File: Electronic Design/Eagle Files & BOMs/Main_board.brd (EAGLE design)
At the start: 99.9 x 69 mm, 35 parts, among them IC2 ATMEGA328-PU, IC3 LM2596S, Q1 IRF9540, Q2 IRF9540, X1 16MHz

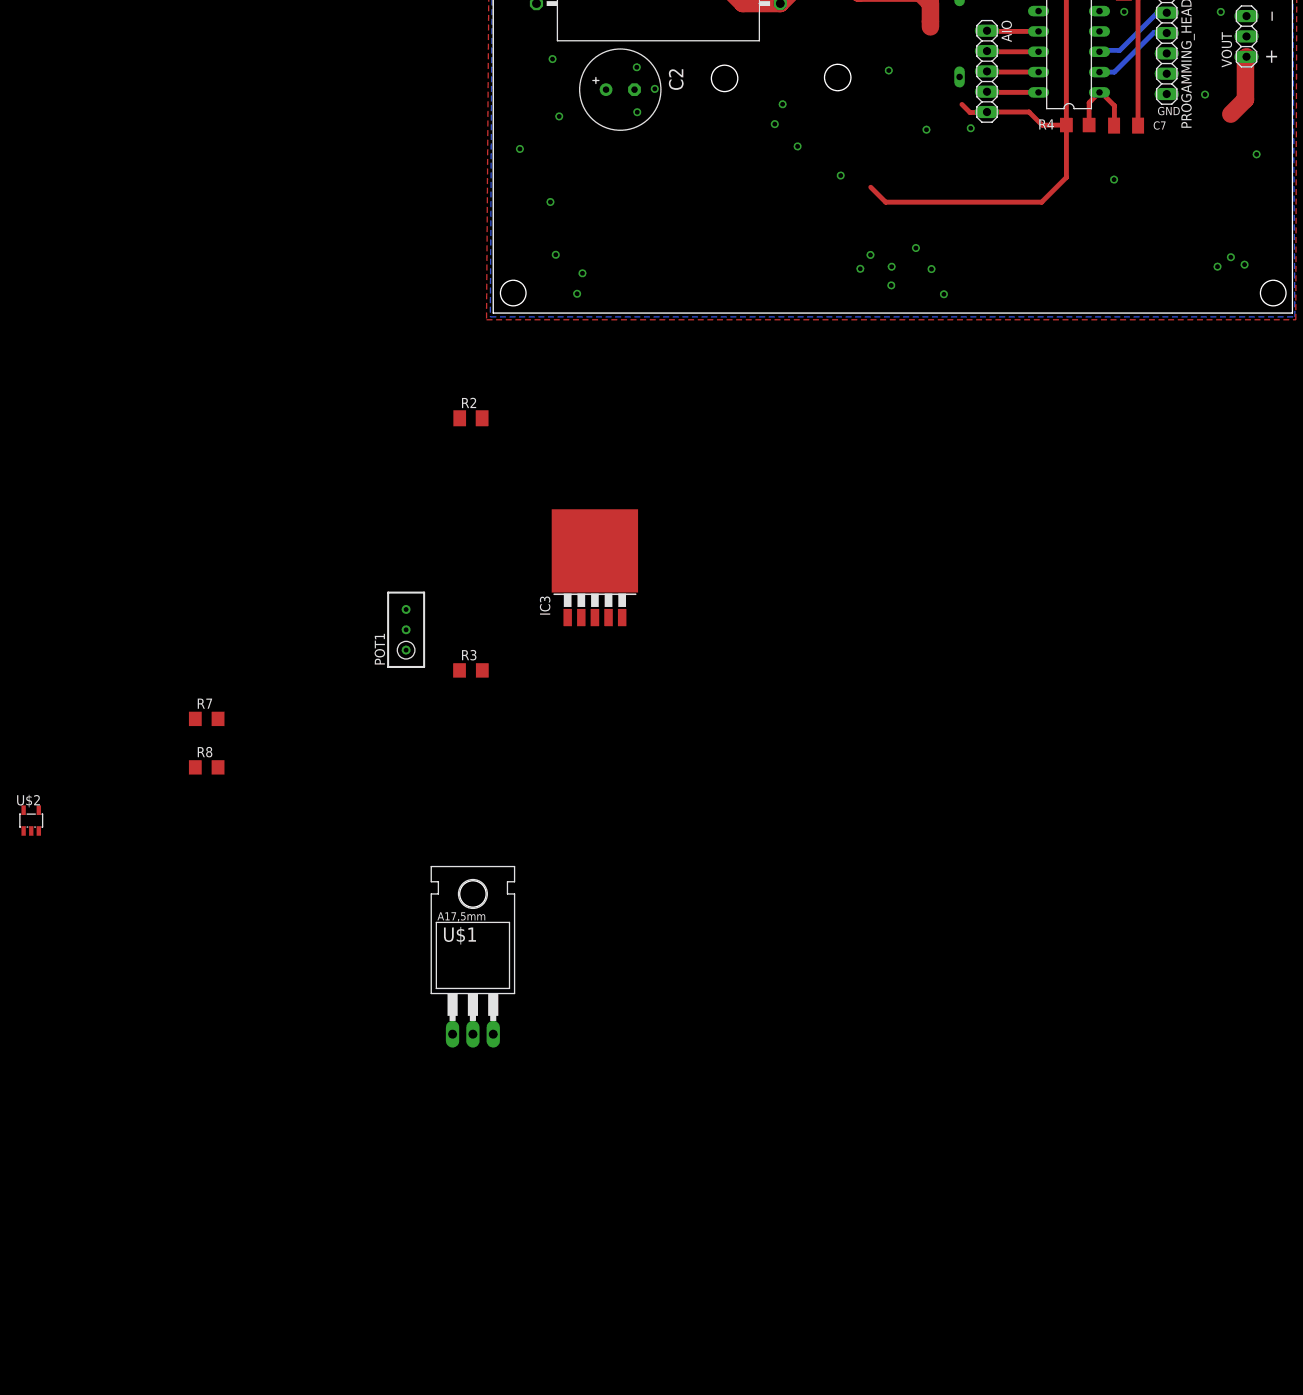
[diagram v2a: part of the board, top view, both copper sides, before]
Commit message: Adding in inductor and feedback to LM2576
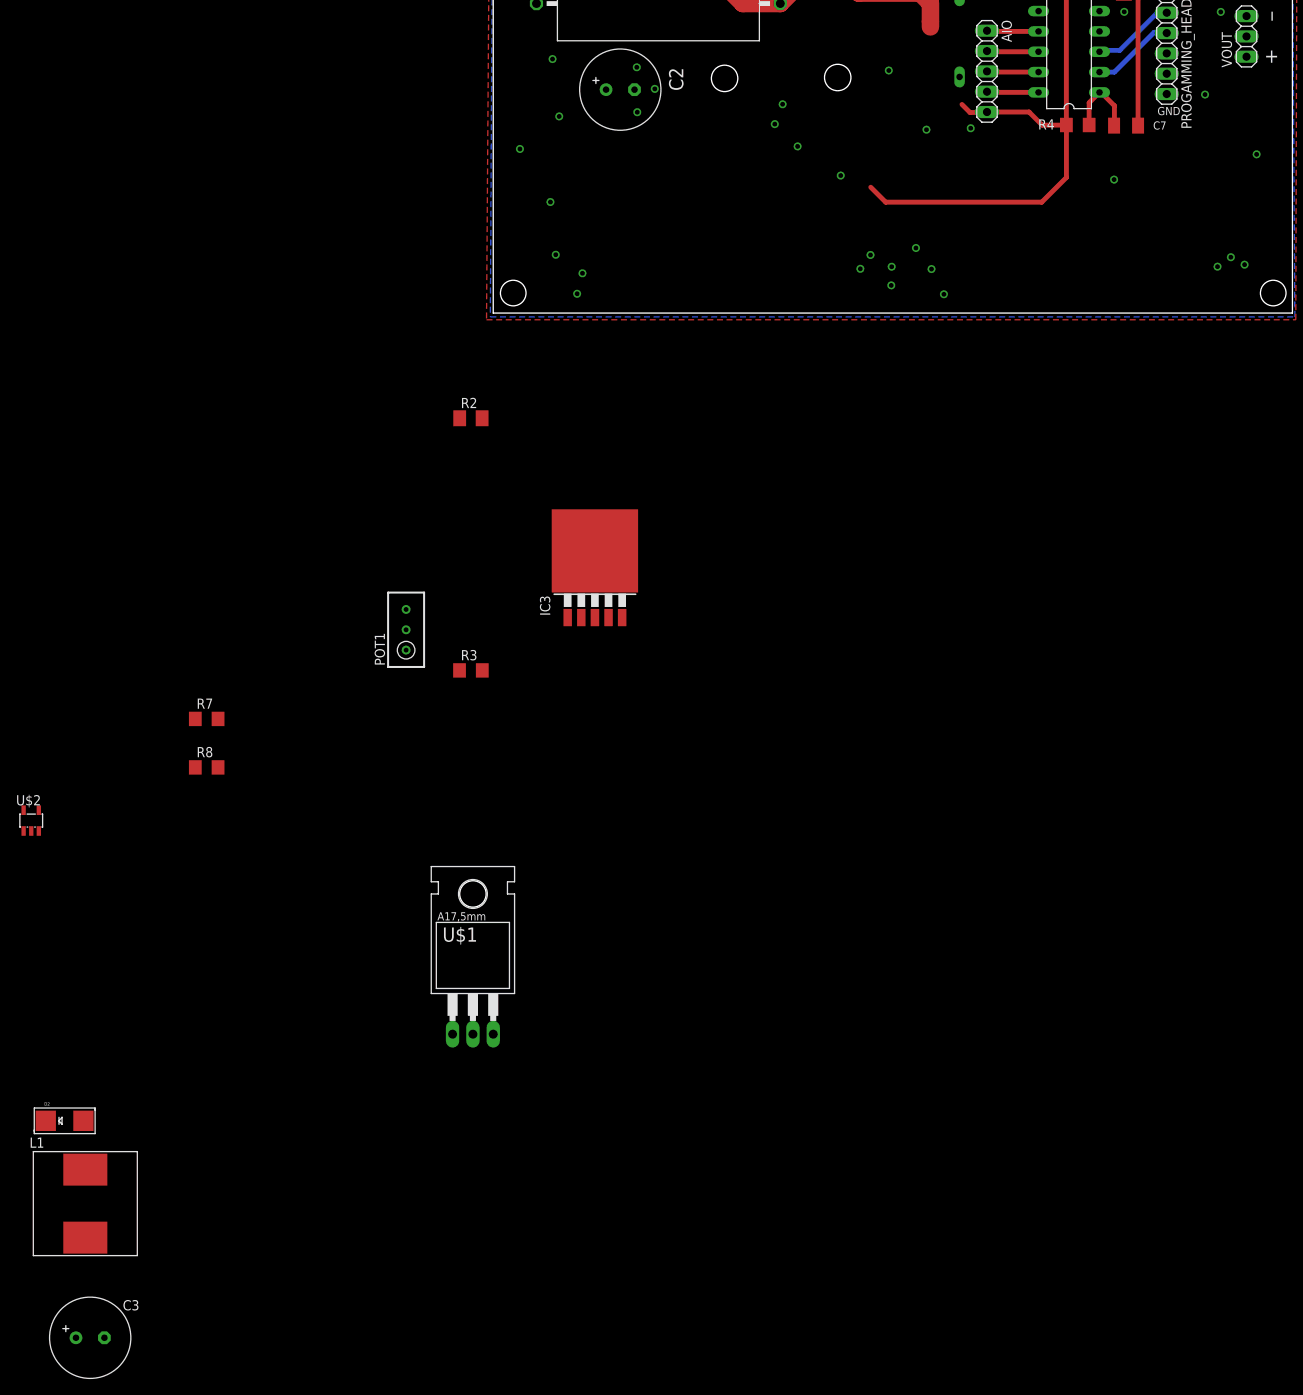
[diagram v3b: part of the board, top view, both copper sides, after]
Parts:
- added C3: 220uF, resistor:E3,5-10
- added D2: (no value), adafruit:SMADIODE
- added L1: MSS1278, Samson:MSS1278
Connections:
- new net N$24: C3.+, L1.P$2, POT1.1, POT1.2, VOUT.1
- net GND: now also C3.-, D2.A
- net M1S: no longer POT1.1, POT1.2
- net N$13: now also D2.C, L1.P$1; no longer VOUT.1
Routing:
- net N$13: track 7.99 -> 0.00 mm

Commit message: replacing lm2596 package with lm2576 package
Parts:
- IC3: value LM2596S -> LM2576S; device national-semiconductor:TO263-5 -> Samson:TO263-5
- moved IC3 115.4 mm to (-3.40, -146.6)
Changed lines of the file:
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@@
 <element name="AIO" library="pinhead" package="1X05" value="" x="61.72" y="30.21" rot="R270"/>
 <element name="R2" library="resistor" package="M1206" value="0R01" x="-2.79" y="-13.15"/>
-<element name="IC3" library="national-semiconductor" package="TO263-5" value="LM2596S" x="12.71" y="-32.27">
-<attribute name="MF" value="NATIONAL SEMICONDUCTOR" x="12.71" y="-32.27" size="1.778" layer="27" display="off"/>
-<attribute name="OC_FARNELL" value="9494367" x="12.71" y="-32.27" size="1.778" layer="27" display="off"/>
-<attribute name="OC_NEWARK" value="41K3842" x="12.71" y="-32.27" size="1.778" layer="27" display="off"/>
-<attribute name="MPN" value="LM2596S-ADJ/NOPB" x="12.71" y="-32.27" size="1.778" layer="27" display="off"/>
+<element name="IC3" library="Samson" package="TO263-5" value="LM2576S" x="-3.4036" y="-146.5812">
+<attribute name="MF" value="NATIONAL SEMICONDUCTOR" x="-3.4036" y="-146.5812" size="1.778" layer="27" display="off"/>
+<attribute name="OC_FARNELL" value="9494367" x="-3.4036" y="-146.5812" size="1.778" layer="27" display="off"/>
+<attribute name="OC_NEWARK" value="41K3842" x="-3.4036" y="-146.5812" size="1.778" layer="27" display="off"/>
+<attribute name="MPN" value="LM2596S-ADJ/NOPB" x="-3.4036" y="-146.5812" size="1.778" layer="27" display="off"/>
 </element>
 <element name="R3" library="resistor" package="R1206" value="2k" x="-2.79" y="-44.67"/>
@@
 <wire x1="-37.242" y1="-56.79" x2="-57.75" y2="-64.74" width="0" layer="19" extent="1-1"/>
 <wire x1="-4.212" y1="-44.67" x2="-37.242" y2="-56.79" width="0" layer="19" extent="1-1"/>
-<wire x1="12.71" y1="-38.0612" x2="-4.212" y2="-44.67" width="0" layer="19" extent="1-1"/>
-<wire x1="16.1136" y1="-38.0612" x2="12.71" y2="-38.0612" width="0" layer="19" extent="1-1"/>
-<wire x1="10.48569375" y1="2.4102" x2="12.71" y2="-38.0612" width="0" layer="19" extent="1-1"/>
+<wire x1="-3.4036" y1="-152.3724" x2="-4.212" y2="-44.67" width="0" layer="19" extent="1-1"/>
+<wire x1="0" y1="-152.3724" x2="-3.4036" y2="-152.3724" width="0" layer="19" extent="1-1"/>
+<wire x1="10.48569375" y1="2.4102" x2="-3.4036" y2="-152.3724" width="0" layer="19" extent="1-1"/>
 <wire x1="11.15569375" y1="4.9702" x2="10.48569375" y2="2.4102" width="0" layer="19" extent="1-1"/>
 <wire x1="7.81569375" y1="7.2902" x2="11.15569375" y2="4.9702" width="0" layer="19" extent="1-1"/>
@@
 <contactref element="U$2" pad="4"/>
 <wire x1="0" y1="-90.14" x2="-56.8" y2="-62.14" width="0" layer="19" extent="1-1"/>
-<wire x1="9.3064" y1="-38.0612" x2="0" y2="-90.14" width="0" layer="19" extent="1-1"/>
-<wire x1="-1.39" y1="-13.15" x2="9.3064" y2="-38.0612" width="0" layer="19" extent="1-1"/>
+<wire x1="-6.8072" y1="-152.3724" x2="0" y2="-90.14" width="0" layer="19" extent="1-1"/>
+<wire x1="-1.39" y1="-13.15" x2="-6.8072" y2="-152.3724" width="0" layer="19" extent="1-1"/>
 </signal>
 <signal name="N$3">
@@
 <contactref element="D2" pad="C"/>
 <wire x1="-55.9295" y1="-100.97" x2="-50.99" y2="-107.07" width="0" layer="19" extent="1-1"/>
-<wire x1="11.0082" y1="-38.0612" x2="-55.9295" y2="-100.97" width="0" layer="19" extent="1-1"/>
+<wire x1="-5.1054" y1="-152.3724" x2="-55.9295" y2="-100.97" width="0" layer="19" extent="1-1"/>
 </signal>
 <signal name="N$2">
@@
 <contactref element="POT1" pad="3"/>
 <wire x1="-1.368" y1="-44.67" x2="-10.89" y2="-37.05" width="0" layer="19" extent="1-1"/>
-<wire x1="14.4118" y1="-38.0612" x2="-1.368" y2="-44.67" width="0" layer="19" extent="1-1"/>
+<wire x1="-1.7018" y1="-152.3724" x2="-1.368" y2="-44.67" width="0" layer="19" extent="1-1"/>
 </signal>
 <signal name="N$24">

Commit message: addig smoothing caps for LM317 out and CS80 inputs
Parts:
- added C4, C5: 0.1u, resistor:C1206K
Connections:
- net +5V: now also C4.1, C5.1
- net GND: now also C4.2, C5.2
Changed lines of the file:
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@@
 <element name="L1" library="Samson" package="MSS1278" value="MSS1278" x="-50.99" y="-111.32"/>
 <element name="C3" library="resistor" package="E3,5-10" value="220uF" x="-50.38" y="-128.09"/>
+<element name="C4" library="resistor" package="C1206K" value="0.1u" x="-57.81" y="-159.31"/>
+<element name="C5" library="resistor" package="C1206K" value="0.1u" x="-57.81" y="-165.98"/>
 </elements>
 <signals>
@@
 <contactref element="D2" pad="A"/>
 <contactref element="C3" pad="-"/>
+<contactref element="C4" pad="2"/>
+<contactref element="C5" pad="2"/>
+<wire x1="-56.31" y1="-159.31" x2="-56.31" y2="-165.98" width="0" layer="19" extent="1-1"/>
+<wire x1="-48.602" y1="-128.09" x2="-56.31" y2="-159.31" width="0" layer="19" extent="1-1"/>
 <wire x1="-51.2305" y1="-100.97" x2="-48.602" y2="-128.09" width="0" layer="19" extent="1-1"/>
 <wire x1="-57.75" y1="-64.74" x2="-51.2305" y2="-100.97" width="0" layer="19" extent="1-1"/>
 <wire x1="-37.242" y1="-56.79" x2="-57.75" y2="-64.74" width="0" layer="19" extent="1-1"/>
 <wire x1="-4.212" y1="-44.67" x2="-37.242" y2="-56.79" width="0" layer="19" extent="1-1"/>
-<wire x1="-3.4036" y1="-152.3724" x2="-4.212" y2="-44.67" width="0" layer="19" extent="1-1"/>
-<wire x1="0" y1="-152.3724" x2="-3.4036" y2="-152.3724" width="0" layer="19" extent="1-1"/>
-<wire x1="10.48569375" y1="2.4102" x2="-3.4036" y2="-152.3724" width="0" layer="19" extent="1-1"/>
+<wire x1="10.48569375" y1="2.4102" x2="-4.212" y2="-44.67" width="0" layer="19" extent="1-1"/>
 <wire x1="11.15569375" y1="4.9702" x2="10.48569375" y2="2.4102" width="0" layer="19" extent="1-1"/>
 <wire x1="7.81569375" y1="7.2902" x2="11.15569375" y2="4.9702" width="0" layer="19" extent="1-1"/>
@@
 <wire x1="34.45569375" y1="52.9802" x2="38.773415625" y2="52.978996875" width="0" layer="19" extent="1-1"/>
 <wire x1="49.50569375" y1="60.0602" x2="38.773415625" y2="52.978996875" width="0" layer="19" extent="1-1"/>
+<wire x1="-3.4036" y1="-152.3724" x2="-48.602" y2="-128.09" width="0" layer="19" extent="1-1"/>
+<wire x1="0" y1="-152.3724" x2="-3.4036" y2="-152.3724" width="0" layer="19" extent="1-1"/>
 </signal>
 <signal name="M1S">
@@
 <contactref element="U$1" pad="2"/>
 <contactref element="U$2" pad="5"/>
-<wire x1="-2.54" y1="-90.14" x2="-58.7" y2="-62.14" width="0" layer="19" extent="1-1"/>
+<contactref element="C4" pad="1"/>
+<contactref element="C5" pad="1"/>
+<wire x1="-59.31" y1="-159.31" x2="-59.31" y2="-165.98" width="0" layer="19" extent="1-1"/>
+<wire x1="-2.54" y1="-90.14" x2="-59.31" y2="-159.31" width="0" layer="19" extent="1-1"/>
 <wire x1="-34.398" y1="-50.73" x2="-2.54" y2="-90.14" width="0" layer="19" extent="1-1"/>
+<wire x1="-58.7" y1="-62.14" x2="-34.398" y2="-50.73" width="0" layer="19" extent="1-1"/>
 <wire x1="47.192" y1="15.728" x2="-34.398" y2="-50.73" width="0" layer="19" extent="1-1"/>
 </signal>

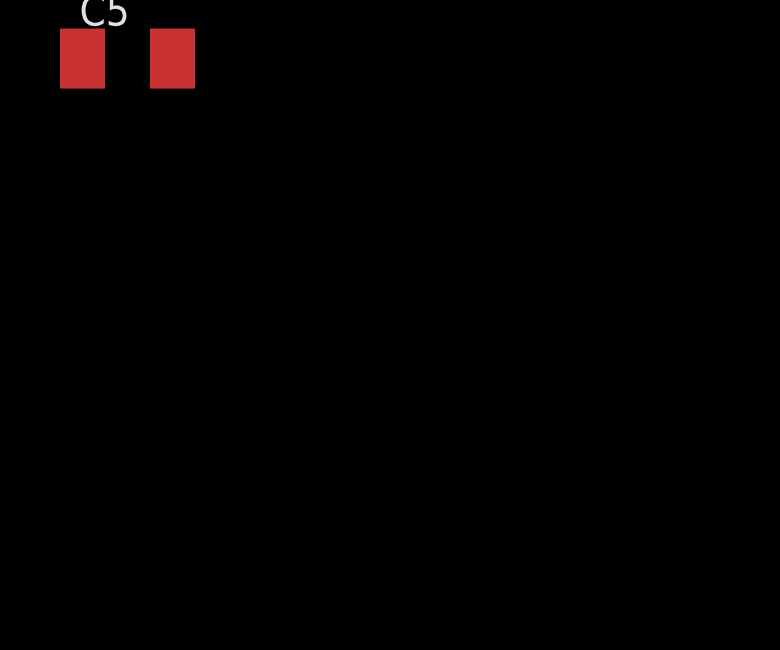
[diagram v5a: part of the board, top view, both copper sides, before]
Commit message: adding smoothing caps and zeners to Iin
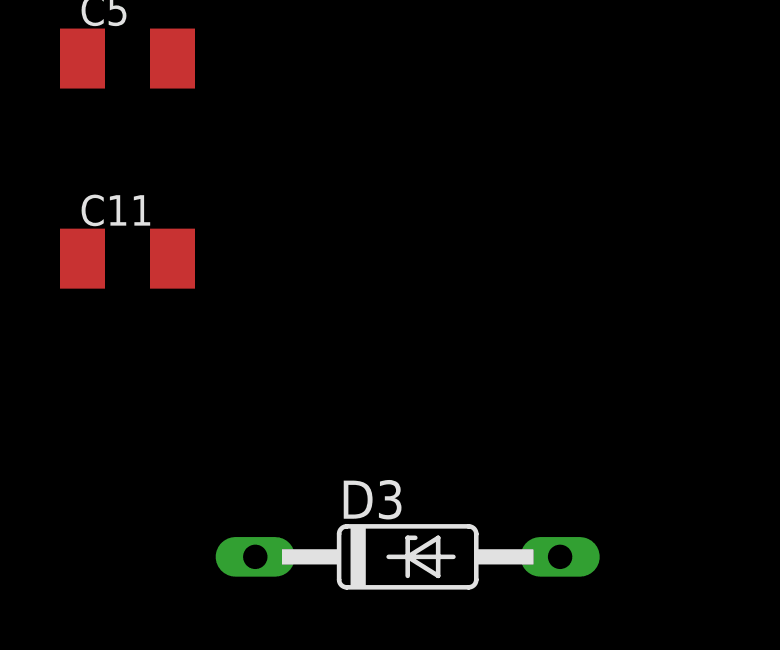
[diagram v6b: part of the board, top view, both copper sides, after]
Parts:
- added C11: 10n, resistor:C1206K
- added D3: 5.1V, diode:DO35Z10
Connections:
- removed net N$2: IC3.4, POT1.3, R3.2
- new net N$26: IC3.4, POT1.2, POT1.3, R3.2
- net GND: now also C11.2, D3.A
- net IIN: now also C11.1, D3.C
- net N$24: no longer POT1.2
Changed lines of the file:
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@@
 <element name="C4" library="resistor" package="C1206K" value="0.1u" x="-57.81" y="-159.31"/>
 <element name="C5" library="resistor" package="C1206K" value="0.1u" x="-57.81" y="-165.98"/>
+<element name="C11" library="resistor" package="C1206K" value="10n" x="-57.81" y="-172.65"/>
+<element name="D3" library="diode" package="DO35Z10" value="5.1V" x="-48.47" y="-182.59"/>
 </elements>
 <signals>
@@
 <wire x1="68.119609375" y1="37.7" x2="68.1625375" y2="37.742928125" width="0.6096" layer="1"/>
 <contactref element="U$2" pad="1"/>
+<contactref element="C11" pad="1"/>
+<contactref element="D3" pad="C"/>
+<wire x1="-59.31" y1="-172.65" x2="-53.55" y2="-182.59" width="0" layer="19" extent="1-1"/>
+<wire x1="-58.7" y1="-64.74" x2="-59.31" y2="-172.65" width="0" layer="19" extent="1-1"/>
 <wire x1="68.119609375" y1="37.7" x2="-58.7" y2="-64.74" width="0" layer="19" extent="1-1"/>
 </signal>
@@
 <contactref element="R3" pad="1"/>
 <contactref element="R8" pad="1"/>
-<contactref element="U$2" pad="2"/>
 <contactref element="D2" pad="A"/>
 <contactref element="C3" pad="-"/>
 <contactref element="C4" pad="2"/>
 <contactref element="C5" pad="2"/>
+<contactref element="C11" pad="2"/>
+<contactref element="D3" pad="A"/>
+<contactref element="U$2" pad="2"/>
+<wire x1="-56.31" y1="-165.98" x2="-56.31" y2="-172.65" width="0" layer="19" extent="1-1"/>
 <wire x1="-56.31" y1="-159.31" x2="-56.31" y2="-165.98" width="0" layer="19" extent="1-1"/>
+<wire x1="-43.39" y1="-182.59" x2="-56.31" y2="-172.65" width="0" layer="19" extent="1-1"/>
 <wire x1="-48.602" y1="-128.09" x2="-56.31" y2="-159.31" width="0" layer="19" extent="1-1"/>
 <wire x1="-51.2305" y1="-100.97" x2="-48.602" y2="-128.09" width="0" layer="19" extent="1-1"/>
@@
 <wire x1="34.45569375" y1="52.9802" x2="38.773415625" y2="52.978996875" width="0" layer="19" extent="1-1"/>
 <wire x1="49.50569375" y1="60.0602" x2="38.773415625" y2="52.978996875" width="0" layer="19" extent="1-1"/>
-<wire x1="-3.4036" y1="-152.3724" x2="-48.602" y2="-128.09" width="0" layer="19" extent="1-1"/>
+<wire x1="-3.4036" y1="-152.3724" x2="-43.39" y2="-182.59" width="0" layer="19" extent="1-1"/>
 <wire x1="0" y1="-152.3724" x2="-3.4036" y2="-152.3724" width="0" layer="19" extent="1-1"/>
 </signal>
@@
 <wire x1="-5.1054" y1="-152.3724" x2="-55.9295" y2="-100.97" width="0" layer="19" extent="1-1"/>
 </signal>
-<signal name="N$2">
-<contactref element="IC3" pad="4"/>
-<contactref element="R3" pad="2"/>
-<contactref element="POT1" pad="3"/>
-<wire x1="-1.368" y1="-44.67" x2="-10.89" y2="-37.05" width="0" layer="19" extent="1-1"/>
-<wire x1="-1.7018" y1="-152.3724" x2="-1.368" y2="-44.67" width="0" layer="19" extent="1-1"/>
-</signal>
 <signal name="N$24">
 <contactref element="L1" pad="P$2"/>
 <contactref element="POT1" pad="1"/>
-<contactref element="POT1" pad="2"/>
 <contactref element="C3" pad="+"/>
 <contactref element="VOUT" pad="1"/>
 <wire x1="-50.99" y1="-115.57" x2="-52.158" y2="-128.09" width="0" layer="19" extent="1-1"/>
 <wire x1="-10.89" y1="-42.13" x2="-50.99" y2="-115.57" width="0" layer="19" extent="1-1"/>
-<wire x1="-10.89" y1="-39.59" x2="-10.89" y2="-42.13" width="0" layer="19" extent="1-1"/>
-<wire x1="94.16" y1="32.04" x2="-10.89" y2="-39.59" width="0" layer="19" extent="1-1"/>
+<wire x1="94.16" y1="32.04" x2="-10.89" y2="-42.13" width="0" layer="19" extent="1-1"/>
+</signal>
+<signal name="N$26">
+<contactref element="POT1" pad="2"/>
+<contactref element="IC3" pad="4"/>
+<contactref element="R3" pad="2"/>
+<contactref element="POT1" pad="3"/>
+<wire x1="-1.368" y1="-44.67" x2="-1.7018" y2="-152.3724" width="0" layer="19" extent="1-1"/>
+<wire x1="-10.89" y1="-39.59" x2="-1.368" y2="-44.67" width="0" layer="19" extent="1-1"/>
+<wire x1="-10.89" y1="-37.05" x2="-10.89" y2="-39.59" width="0" layer="19" extent="1-1"/>
 </signal>
 </signals>

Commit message: adding hardwired voltage divider for Vin measurement
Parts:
- removed POT2: 500k, resistor:RTRIM3296W
- added R10: 21k5, resistor:R0805
- added R9: 1k13, resistor:R0805
- C3: value 220uF -> 1000uF
- moved IC3 176.3 mm to (80.5, 8.50), turned to 270 degrees
- moved C2 35.5 mm to (50.6, 35.3), turned to 270 degrees
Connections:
- net GND: now also R10.1; no longer POT2.1
- net N$3: now also R9.2; no longer POT2.3
- net VIN: now also R10.2, R9.1; no longer POT2.2
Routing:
- net N$3: track 25.8 -> 24.7 mm
